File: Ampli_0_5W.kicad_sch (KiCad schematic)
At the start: 69 parts, among them J1 RF_In, J2 PTT_In, J3 Aux_PTT_Out, J4 RF_Out, Q1 2N7002, Q2 FDD6685, Q3 2N5109, Q4 AFT05MP075N, Q5 2SC5551A, T1 4:1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

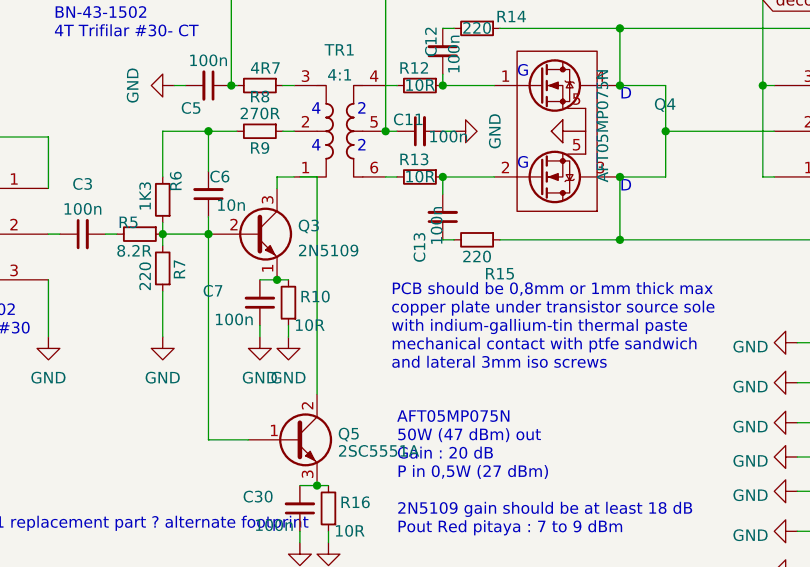
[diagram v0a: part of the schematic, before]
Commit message: new slotted pcb, new transistor added
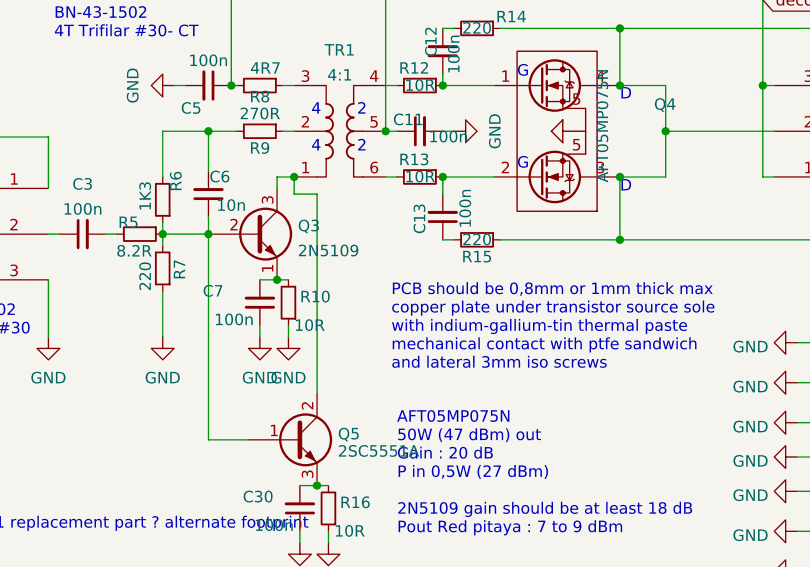
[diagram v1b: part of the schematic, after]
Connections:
- net at Q3.3 (C), TR1.1: now also Q5.2 (C)
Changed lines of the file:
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@@
   (junction (at 50.165 59.69) (diameter 0) (color 0 0 0 0)
   )
+  (junction (at 80.01 103.505) (diameter 0) (color 0 0 0 0)
+  )
   (junction (at 70.485 109.855) (diameter 0) (color 0 0 0 0)
   )
@@
     (stroke (width 0) (type default))
   )
-  (wire (pts (xy 80.645 103.505) (xy 82.55 103.505))
-    (stroke (width 0) (type default))
-  )
   (wire (pts (xy 90.17 52.705) (xy 91.44 52.705))
     (stroke (width 0) (type default))
@@
     (stroke (width 0) (type default))
   )
+  (wire (pts (xy 80.01 105.41) (xy 80.01 103.505))
+    (stroke (width 0) (type default))
+  )
   (wire (pts (xy 179.705 99.06) (xy 179.705 105.41))
     (stroke (width 0) (type default))
@@
     (stroke (width 0) (type default))
   )
-  (wire (pts (xy 82.55 103.505) (xy 82.55 127.635))
-    (stroke (width 0) (type default))
-  )
   (wire (pts (xy 158.75 51.435) (xy 158.75 52.705))
     (stroke (width 0) (type default))
@@
     (stroke (width 0) (type default))
   )
+  (wire (pts (xy 82.55 105.41) (xy 80.01 105.41))
+    (stroke (width 0) (type default))
+  )
   (wire (pts (xy 73.025 46.99) (xy 114.935 46.99))
     (stroke (width 0) (type default))
@@
   )
   (wire (pts (xy 137.795 147.32) (xy 135.89 147.32))
+    (stroke (width 0) (type default))
+  )
+  (wire (pts (xy 82.55 127.635) (xy 82.55 105.41))
     (stroke (width 0) (type default))
   )
@@
   (text "https://ludens.cl/Electron/50Wamp/RP50Wampwm.png\n\nhttps://ludens.cl/Electron/50Wamp/50Wamp.html\n\nAutor : XQ6FOD Manfred\n"
     (at 177.8 178.435 0)
-    (effects (font (size 1.27 1.27)) (justify left bottom))
+    (effects (font (size 1.27 1.27)) (justify left bottom) (href "https://ludens.cl/Electron/50Wamp/50Wamp.html"))
   )
   (text "2\n\n2\n" (at 86.995 100.965 0)
@@
   (symbol (lib_id "Device:R_Small") (at 100.33 110.49 270) (unit 1)
     (in_bom yes) (on_board yes) (dnp no)
-    (property "Reference" "R15" (at 102.87 114.3 90)
-      (effects (font (size 1.27 1.27)))
-    )
-    (property "Value" "220" (at 100.33 112.395 90)
+    (property "Reference" "R15" (at 100.33 112.395 90)
+      (effects (font (size 1.27 1.27)))
+    )
+    (property "Value" "220" (at 100.33 110.49 90)
       (effects (font (size 1.27 1.27)))
     )
@@
   (symbol (lib_id "Device:C_Small") (at 96.52 107.95 180) (unit 1)
     (in_bom yes) (on_board yes) (dnp no)
-    (property "Reference" "C13" (at 93.98 113.03 90)
+    (property "Reference" "C13" (at 93.98 109.855 90)
       (effects (font (size 1.27 1.27)) (justify right))
     )
-    (property "Value" "100n" (at 95.885 111.125 90)
+    (property "Value" "100n" (at 99.06 109.22 90)
       (effects (font (size 1.27 1.27)) (justify right))
     )
